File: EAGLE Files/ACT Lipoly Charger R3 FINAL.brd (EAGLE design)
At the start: 94 x 53 mm, 150 parts, among them J12 Bk, J13 Sel, J14 Fwd, U1 74HC595

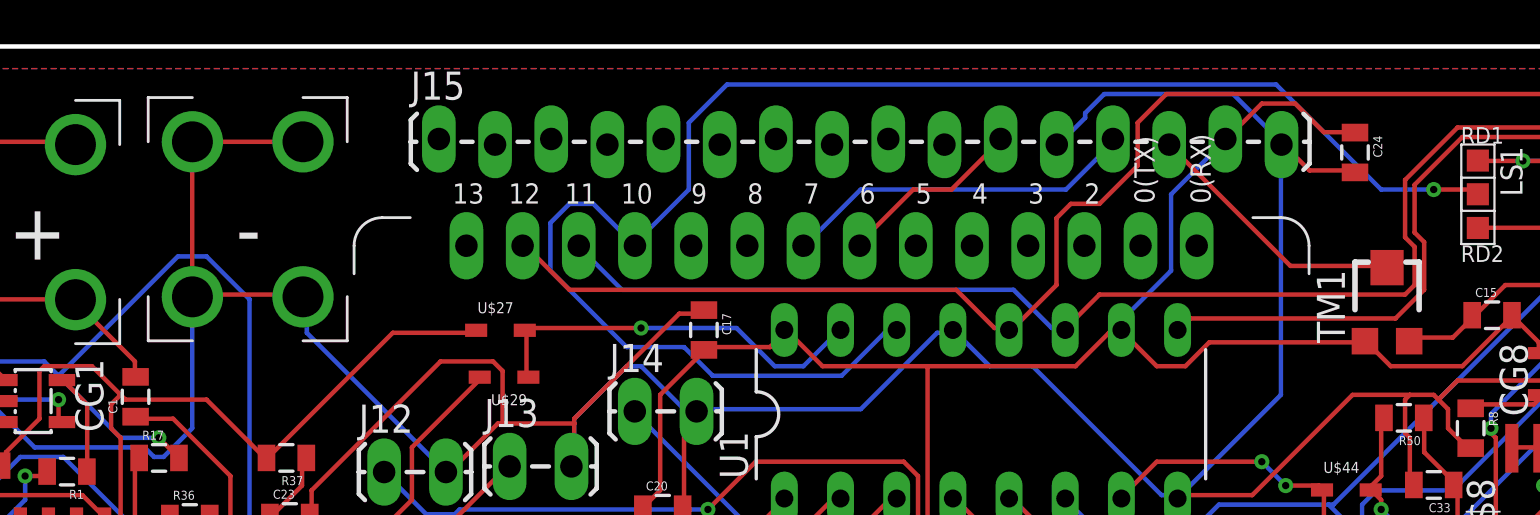
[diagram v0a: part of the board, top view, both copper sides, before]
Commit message: Adds missing LCD signal traces
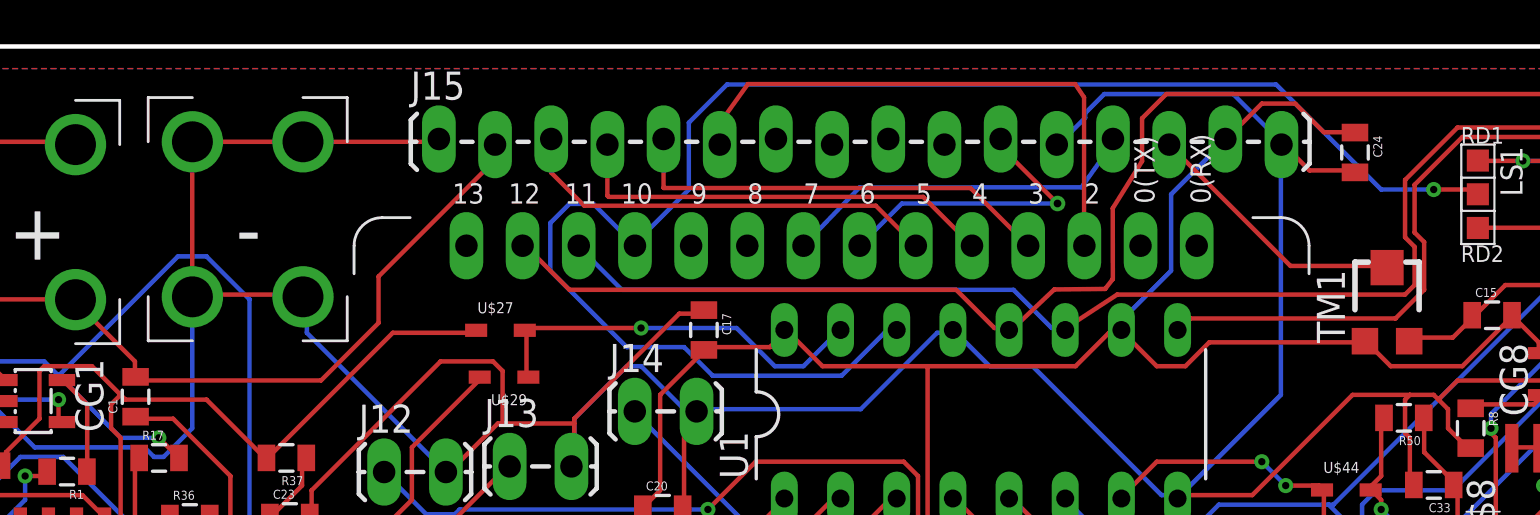
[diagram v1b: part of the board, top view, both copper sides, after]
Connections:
- net D2: now also J15.6
- net D3: now also J15.5
- net D4: now also J15.4
- net D5: now also J15.3
- net GND: now also J15.1
- net VCC: now also J15.2
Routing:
- net D2: track 0.00 -> 25.4 mm
- net VCC: track 476.6 -> 499.0 mm
- net D5: track 0.00 -> 20.9 mm
- net D3: track 0.00 -> 19.8 mm
- net D4: track 0.00 -> 19.7 mm
- net GND: track 689.3 -> 695.5 mm
- net D6: track 8.45 -> 14.0 mm, vias 0 -> 1
- net D7: track 16.1 -> 16.6 mm
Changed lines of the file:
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@@
 <?xml version="1.0" encoding="utf-8"?>
 <!DOCTYPE eagle SYSTEM "eagle.dtd">
-<eagle version="7.7.0">
+<eagle version="8.2.2">
 <drawing>
 <settings>
@@
 <setting verticaltext="up"/>
 </settings>
-<grid distance="1" unitdist="mm" unit="mm" style="lines" multiple="1" display="yes" altdistance="0.025" altunitdist="inch" altunit="inch"/>
+<grid distance="0.1" unitdist="mm" unit="mm" style="lines" multiple="1" display="yes" altdistance="0.025" altunitdist="inch" altunit="inch"/>
 <layers>
 <layer number="1" name="Top" color="4" fill="1" visible="yes" active="yes"/>
@@
 <vertex x="26" y="62"/>
 </polygon>
+<contactref element="J15" pad="1"/>
+<wire x1="55.60701875" y1="63.79701875" x2="55.627" y2="63.817" width="0.1524" layer="1"/>
+<wire x1="49.483" y1="63.69" x2="55.5" y2="63.69" width="0.2" layer="1"/>
+<wire x1="55.5" y1="63.69" x2="55.60701875" y2="63.79701875" width="0.2" layer="1"/>
 </signal>
 <signal name="VCC">
@@
 <wire x1="41.8846" y1="53.7591" x2="41.8846" y2="53.1114" width="0.2032" layer="1"/>
 <wire x1="39.2938" y1="56.3499" x2="41.8846" y2="53.7591" width="0.2032" layer="1"/>
-<wire x1="41.8846" y1="53.1114" x2="41.913" y2="53.061" width="0.2032" layer="1"/>
+<wire x1="41.913" y1="53.061" x2="41.8846" y2="53.1114" width="0.2032" layer="1"/>
 <wire x1="39.2938" y1="56.3499" x2="39.196" y2="56.553" width="0.2032" layer="1"/>
 <wire x1="30.6578" y1="43.3959" x2="31.9532" y2="43.3959" width="0.2032" layer="1"/>
@@
 <wire x1="114.2111" y1="34.544" x2="112.75" y2="36" width="0.2032" layer="1"/>
 <via x="107.5" y="25.5" extent="1-16" drill="0.6"/>
+<contactref element="J15" pad="2"/>
+<wire x1="58.167" y1="63.563" x2="58.167" y2="62.867" width="0.2" layer="1"/>
+<wire x1="58.167" y1="62.867" x2="52.9" y2="57.6" width="0.2" layer="1"/>
+<wire x1="52.9" y1="57.6" x2="52.9" y2="55.5" width="0.2" layer="1"/>
+<wire x1="50.3" y1="52.9" x2="42.074" y2="52.9" width="0.2" layer="1"/>
+<wire x1="42.074" y1="52.9" x2="41.913" y2="53.061" width="0.2" layer="1"/>
+<wire x1="52.9" y1="55.5" x2="50.3" y2="52.9" width="0.2" layer="1"/>
+<wire x1="107.3023" y1="39.0779" x2="109.4613" y2="39.0779" width="0" layer="19" extent="1-16"/>
+<wire x1="107.5" y1="25.5" x2="108.085" y2="24.9141" width="0" layer="19" extent="1-1"/>
+<wire x1="39.77" y1="26.43" x2="42.48" y2="25.415" width="0" layer="19" extent="1-1"/>
+<wire x1="76.27" y1="18.03" x2="72.96" y2="23.715" width="0" layer="19" extent="1-1"/>
 </signal>
 <signal name="CHG8">
@@
 <wire x1="112.0521" y1="65.8495" x2="114.8588" y2="63.0428" width="0.2032" layer="1"/>
 <wire x1="88.519" y1="65.8495" x2="112.0521" y2="65.8495" width="0.2032" layer="1"/>
-<wire x1="87.2236" y1="64.5541" x2="88.519" y2="65.8495" width="0.2032" layer="1"/>
-<wire x1="87.2236" y1="62.611" x2="87.2236" y2="64.5541" width="0.2032" layer="1"/>
-<wire x1="85.4964" y1="60.8838" x2="87.2236" y2="62.611" width="0.2032" layer="1"/>
-<wire x1="84.201" y1="60.8838" x2="85.4964" y2="60.8838" width="0.2032" layer="1"/>
-<wire x1="83.5533" y1="60.2361" x2="84.201" y2="60.8838" width="0.2032" layer="1"/>
-<wire x1="83.5533" y1="57.2135" x2="83.5533" y2="60.2361" width="0.2032" layer="1"/>
-<wire x1="81.6102" y1="55.2704" x2="83.5533" y2="57.2135" width="0.2032" layer="1"/>
+<wire x1="87.4236" y1="64.7541" x2="88.519" y2="65.8495" width="0.2032" layer="1"/>
+<wire x1="87.4236" y1="62.811" x2="87.4236" y2="64.7541" width="0.2032" layer="1"/>
+<wire x1="86.0964" y1="60.6838" x2="87.4236" y2="62.811" width="0.2032" layer="1"/>
+<wire x1="86.101" y1="57.4838" x2="86.0964" y2="60.6838" width="0.2032" layer="1"/>
+<wire x1="85.7533" y1="57.0361" x2="86.101" y2="57.4838" width="0.2032" layer="1"/>
+<wire x1="83.4533" y1="57.0135" x2="85.7533" y2="57.0361" width="0.2032" layer="1"/>
+<wire x1="81.6102" y1="55.2704" x2="83.4533" y2="57.0135" width="0.2032" layer="1"/>
 <wire x1="113.5634" y1="60.0202" x2="113.531" y2="59.825" width="0.2032" layer="1"/>
 <wire x1="81.6102" y1="55.2704" x2="81.408" y2="55.181" width="0.2032" layer="1"/>
@@
 <contactref element="U$17" pad="7"/>
 <contactref element="J15" pad="13"/>
-<wire x1="74.7014" y1="61.5315" x2="72.3265" y2="59.1566" width="0.2032" layer="16"/>
-<wire x1="83.9851" y1="61.5315" x2="74.7014" y2="61.5315" width="0.2032" layer="16"/>
-<wire x1="86.1441" y1="63.6905" x2="83.9851" y2="61.5315" width="0.2032" layer="16"/>
-<wire x1="72.3265" y1="59.1566" x2="72.113" y2="58.991" width="0.2032" layer="16"/>
+<wire x1="86.1441" y1="63.6905" x2="84.6851" y2="61.6315" width="0.2032" layer="16"/>
+<wire x1="72.113" y1="58.991" x2="72.3265" y2="59.1566" width="0.2032" layer="16"/>
 <wire x1="86.1441" y1="63.6905" x2="86.107" y2="63.817" width="0.2032" layer="16"/>
+<wire x1="84.6851" y1="61.6315" x2="74.6535" y2="61.6315" width="0.2" layer="16"/>
+<wire x1="74.6535" y1="61.6315" x2="72.113" y2="58.991" width="0.2" layer="16"/>
 </signal>
 <signal name="D6">
 <contactref element="U$17" pad="6"/>
 <contactref element="J15" pad="11"/>
-<wire x1="77.0763" y1="61.5315" x2="74.7014" y2="59.1566" width="0.2032" layer="1"/>
-<wire x1="78.8035" y1="61.5315" x2="77.0763" y2="61.5315" width="0.2032" layer="1"/>
-<wire x1="80.9625" y1="63.6905" x2="78.8035" y2="61.5315" width="0.2032" layer="1"/>
 <wire x1="74.7014" y1="59.1566" x2="74.653" y2="58.991" width="0.2032" layer="1"/>
 <wire x1="80.9625" y1="63.6905" x2="81.027" y2="63.817" width="0.2032" layer="1"/>
+<wire x1="81.027" y1="63.817" x2="81.027" y2="63.473" width="0.2" layer="1"/>
+<wire x1="81.027" y1="63.473" x2="83.6" y2="60.9" width="0.2" layer="1"/>
+<via x="83.6" y="60.9" extent="1-16" drill="0.35"/>
+<wire x1="83.6" y1="60.9" x2="76.562" y2="60.9" width="0.2" layer="16"/>
+<wire x1="76.562" y1="60.9" x2="74.653" y2="58.991" width="0.2" layer="16"/>
 </signal>
 <signal name="D5">
 <contactref element="U$17" pad="5"/>
+<contactref element="J15" pad="3"/>
+<wire x1="60.707" y1="62.293" x2="60.707" y2="63.817" width="0.1524" layer="1"/>
+<wire x1="60.707" y1="63.817" x2="60.707" y2="62.293" width="0.2" layer="1"/>
+<wire x1="60.707" y1="62.293" x2="62.2" y2="60.8" width="0.2" layer="1"/>
+<wire x1="62.2" y1="60.8" x2="75.384" y2="60.8" width="0.2" layer="1"/>
+<wire x1="75.384" y1="60.8" x2="77.193" y2="58.991" width="0.2" layer="1"/>
 </signal>
 <signal name="D4">
 <contactref element="U$17" pad="4"/>
+<contactref element="J15" pad="4"/>
+<wire x1="63.247" y1="63.563" x2="63.247" y2="61.253" width="0.2" layer="1"/>
+<wire x1="63.247" y1="61.253" x2="63.3" y2="61.2" width="0.2" layer="1"/>
+<wire x1="63.3" y1="61.2" x2="77.524" y2="61.2" width="0.2" layer="1"/>
+<wire x1="77.524" y1="61.2" x2="79.733" y2="58.991" width="0.2" layer="1"/>
 </signal>
 <signal name="D3">
 <contactref element="U$17" pad="3"/>
+<contactref element="J15" pad="5"/>
+<wire x1="65.787" y1="63.817" x2="65.787" y2="61.613" width="0.2" layer="1"/>
+<wire x1="65.787" y1="61.613" x2="65.8" y2="61.6" width="0.2" layer="1"/>
+<wire x1="65.8" y1="61.6" x2="79.664" y2="61.6" width="0.2" layer="1"/>
+<wire x1="79.664" y1="61.6" x2="82.273" y2="58.991" width="0.2" layer="1"/>
 </signal>
 <signal name="D2">
 <contactref element="U$17" pad="2"/>
+<contactref element="J15" pad="6"/>
+<wire x1="68.327" y1="63.563" x2="68.327" y2="64.527" width="0.2" layer="1"/>
+<wire x1="68.327" y1="64.527" x2="69.6" y2="66.3" width="0.2" layer="1"/>
+<wire x1="69.6" y1="66.3" x2="84.4" y2="66.3" width="0.2" layer="1"/>
+<wire x1="84.4" y1="66.3" x2="84.8" y2="65.7" width="0.2" layer="1"/>
+<wire x1="84.8" y1="59.278" x2="84.813" y2="58.991" width="0.2" layer="1"/>
+<wire x1="84.8" y1="65.7" x2="84.8" y2="59.278" width="0.2" layer="1"/>
 </signal>
 <signal name="A1">
@@
 <wire x1="99.7458" y1="57.2135" x2="99.7458" y2="58.9407" width="0.2032" layer="1"/>
 <wire x1="99.314" y1="56.7817" x2="99.7458" y2="57.2135" width="0.2032" layer="1"/>
-<wire x1="85.4964" y1="56.7817" x2="99.314" y2="56.7817" width="0.2032" layer="1"/>
-<wire x1="83.9851" y1="55.2704" x2="85.4964" y2="56.7817" width="0.2032" layer="1"/>
+<wire x1="86.2964" y1="56.7817" x2="99.314" y2="56.7817" width="0.2032" layer="1"/>
+<wire x1="83.9851" y1="55.2704" x2="86.2964" y2="56.7817" width="0.2032" layer="1"/>
 <wire x1="113.3475" y1="62.3951" x2="113.531" y2="62.365" width="0.2032" layer="1"/>
 <wire x1="83.9851" y1="55.2704" x2="83.948" y2="55.181" width="0.2032" layer="1"/>
